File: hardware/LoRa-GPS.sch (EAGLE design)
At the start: 26 parts, among them J2 MF-CON-MICROUSB-RIGHT, U1 MCP1703-3302E/CB, Y1 CRYSTAL.ABS07

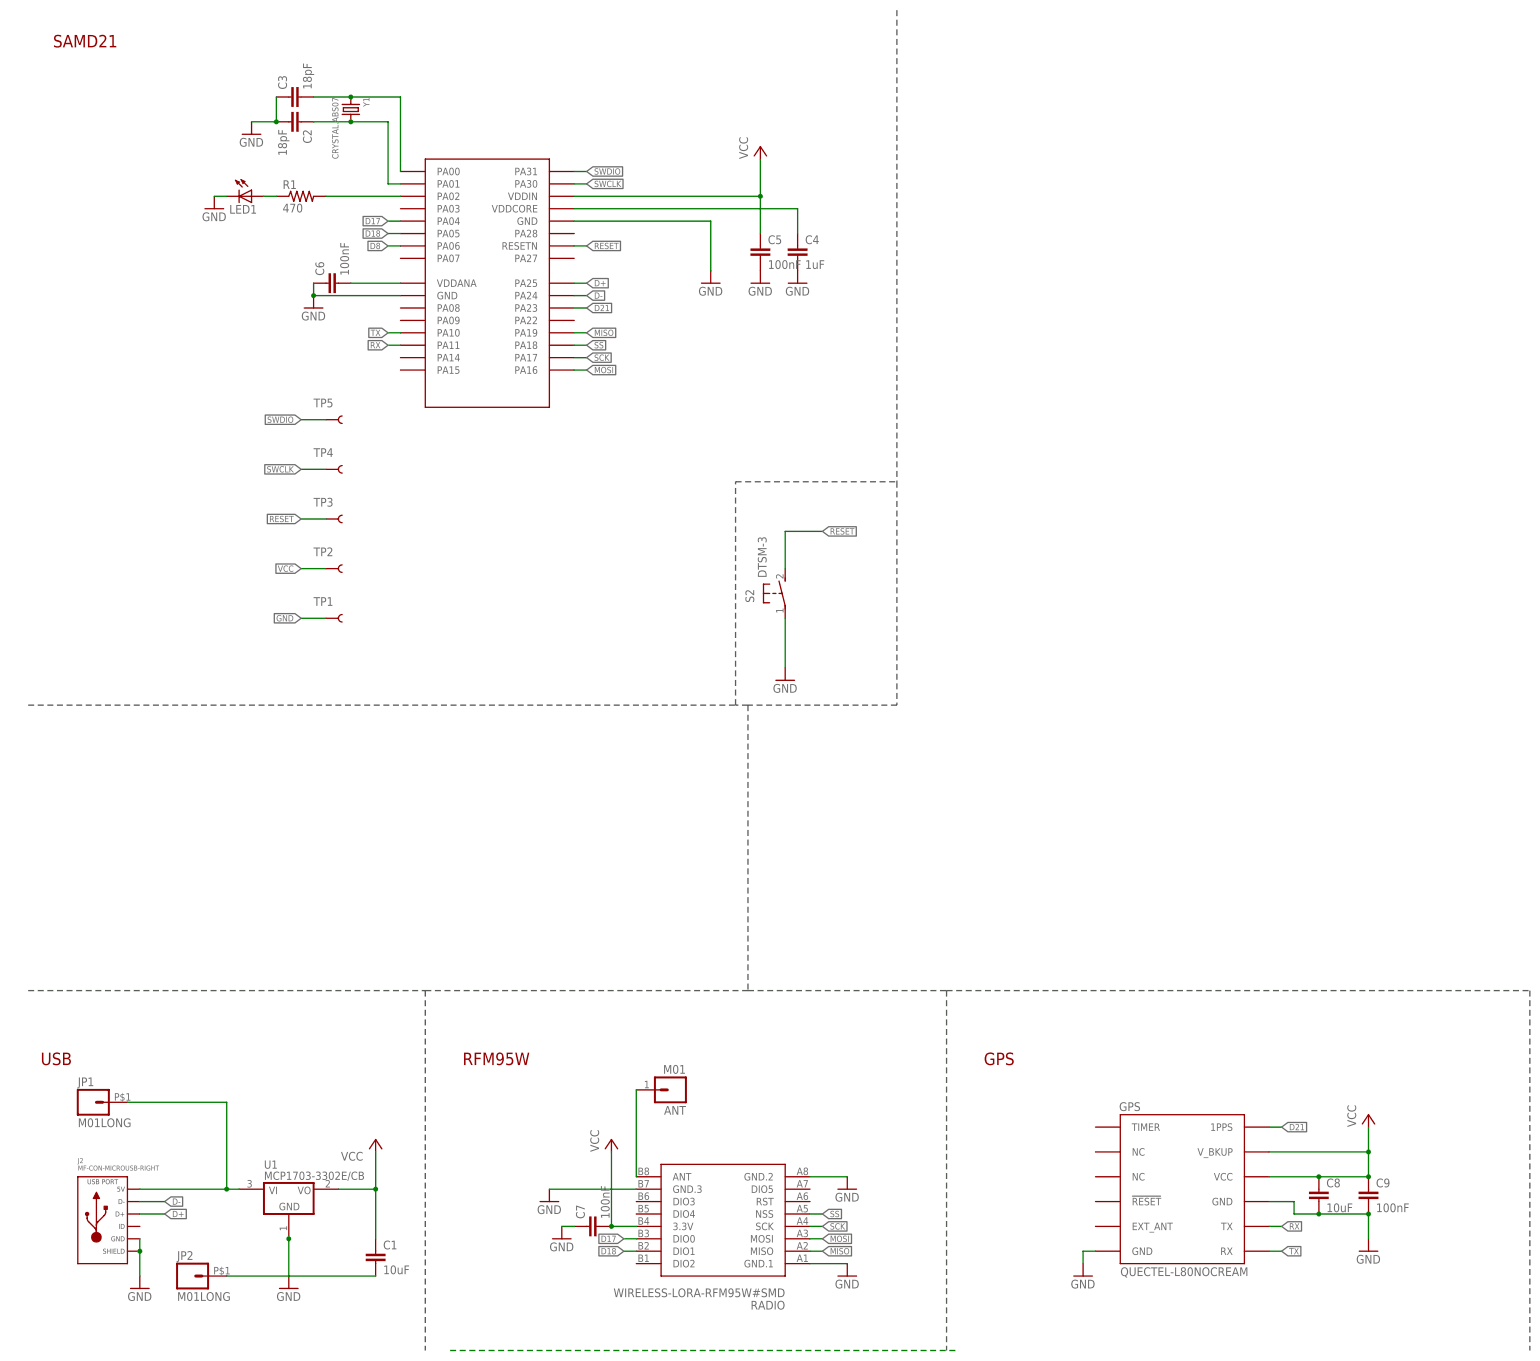
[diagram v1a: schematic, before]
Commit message: add GPS VCC switch - check CPU pin is ok?
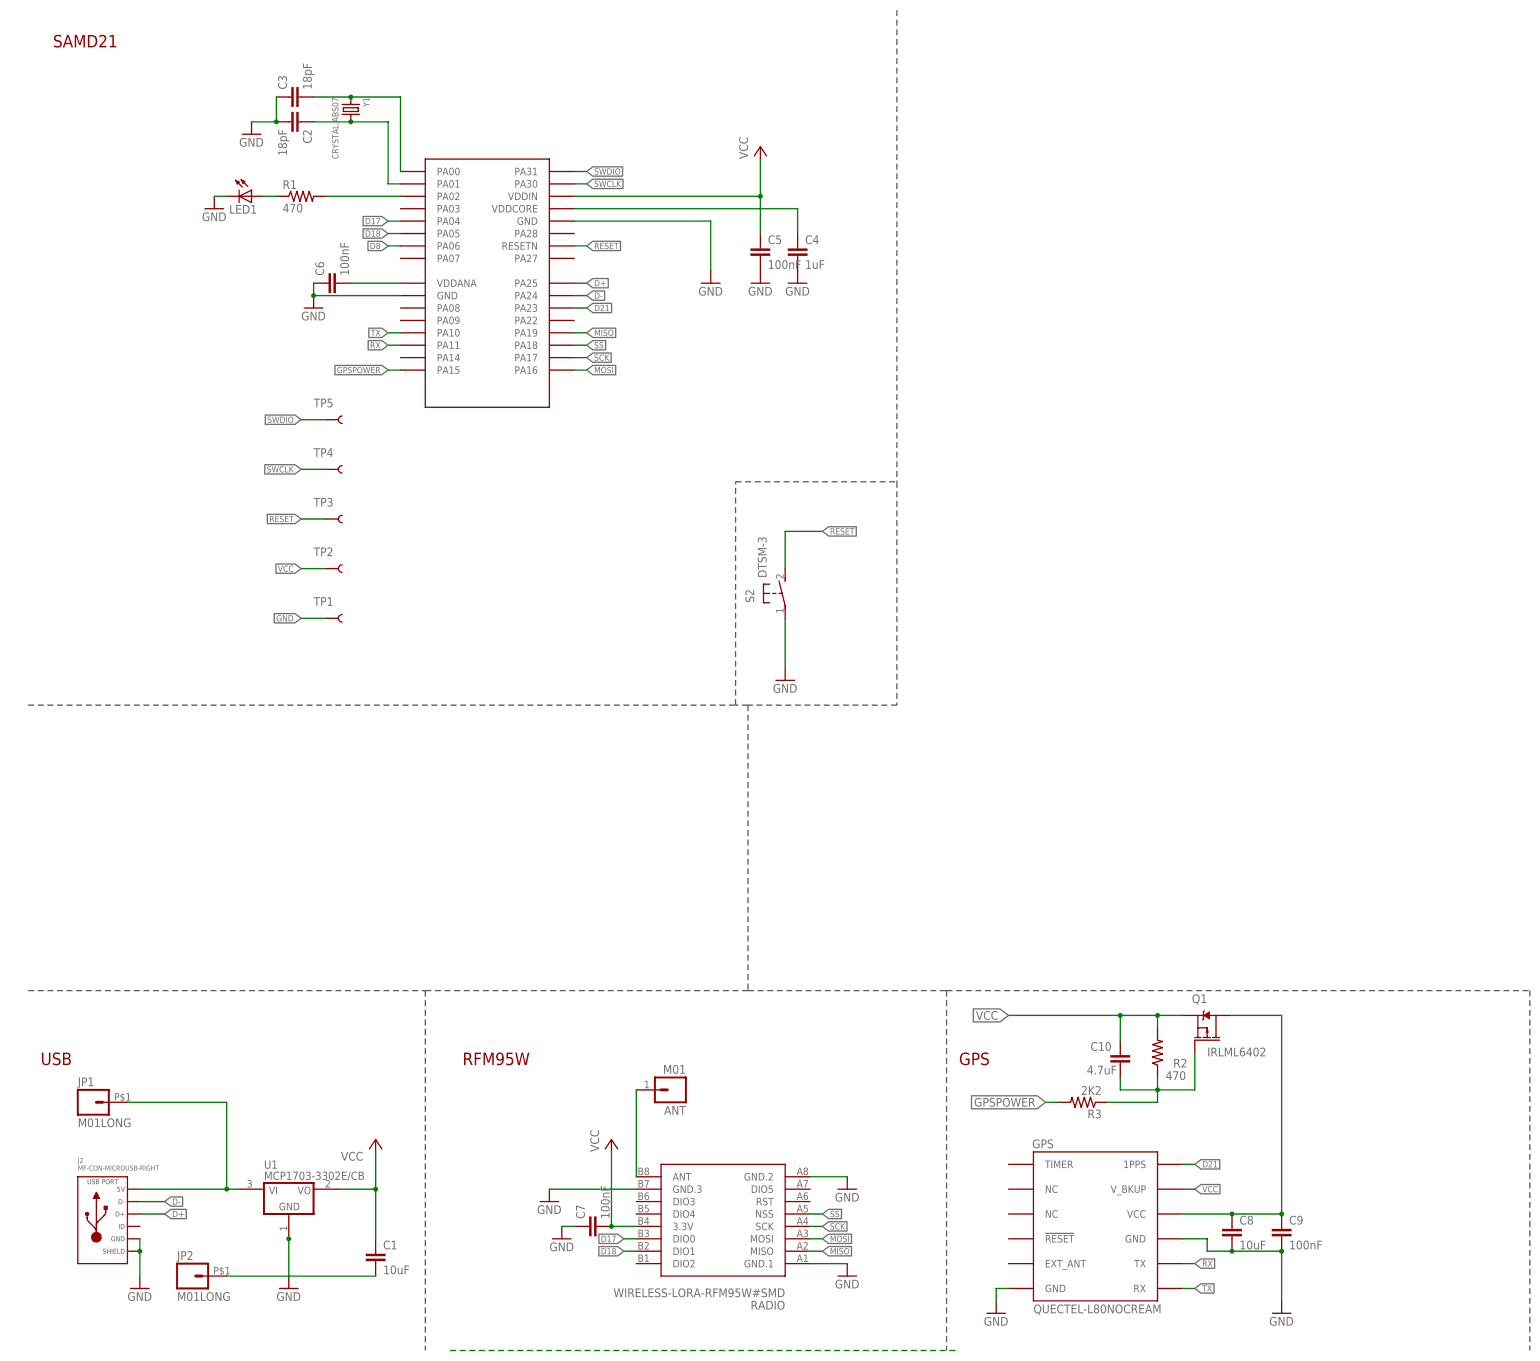
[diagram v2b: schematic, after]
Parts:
- added C10: 4.7uF, nootropicdesign:CAPC0603-THINCREAM
- added Q1: IRLML6402, ianc:MOSFET_PCH-IRLML6402
- added R2: 470, nootropicdesign:R-USR0603-THINCREAM
- added R3: 2K2, nootropicdesign:R-USR0603-THINCREAM
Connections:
- new net GPSPOWER: R3.2, SAMD21.PA15
- new net N$7: C8.1, C9.1, GPS.VCC, Q1.D
- new net N$8: C10.2, Q1.G, R2.1, R3.1
- net VCC: now also C10.1, Q1.S, R2.2; no longer C8.1, C9.1, GPS.VCC
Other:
- moved on the sheet: C8, C9, GPS

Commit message: amph usb conn
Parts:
- removed J2: MF-CON-MICROUSB-RIGHT, nootropicdesign:USB_MICRO_RIGHT
- added J1: 10118193-0001LF, usb:10118193-0001LF
- ANT, C1, C10, C2, C3, C4, C8, GPS, JP1, JP2, LED1, Q1, R1, R2, R3, RADIO, S2, SAMD21, TP1, TP2, TP3, TP4, TP5, U1, Y1: OC_FARNELL (none) -> unknown
- C5, C6, C7, C9: MF (none) -> AVX; MPN (none) -> 02016D104KAT2A; OC_FARNELL (none) -> 1657913
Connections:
- net D+: now also J1.3; no longer J2.D+
- net D-: now also J1.2; no longer J2.D-
- net GND: now also J1.5; no longer J2.GND, J2.SLD
- net VIN: now also J1.1; no longer J2.5V

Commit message: 470 to 47k
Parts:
- R2: value 470 -> 47k
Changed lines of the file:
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@@
 <attribute name="OC_FARNELL" value="unknown"/>
 </part>
-<part name="R2" library="nootropicdesign" deviceset="R-US" device="R0603-THINCREAM" value="470">
+<part name="R2" library="nootropicdesign" deviceset="R-US" device="R0603-THINCREAM" value="47k">
 <attribute name="MF" value=""/>
 <attribute name="MPN" value=""/>

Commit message: sma
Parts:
- removed J1: 10118193-0001LF, usb:10118193-0001LF
- added J2: CON-SMA-EDGE-S, CON-SMA-EDGE-S:CON-SMA-EDGE-S
- added J3: USB3085-XX-X_REVD, USB3085-XX-X_REVD:USB3085-XX-X_REVD
- ANT: value M01 -> (none); device nootropicdesign:M01 -> wirepad:1,6/0,8; OC_FARNELL unknown -> (none)
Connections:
- net ANT: now also ANT.P, J2.1; no longer ANT.1
- net D+: now also J3.D+; no longer J1.3
- net D-: now also J3.D-; no longer J1.2
- net GND: now also J2.2, J3.GND; no longer J1.5
- net VIN: now also J3.VBUS; no longer J1.1
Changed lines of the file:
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@@
 <layer number="2" name="Route2" color="1" fill="3" visible="no" active="no"/>
 <layer number="3" name="Route3" color="4" fill="3" visible="no" active="no"/>
+<layer number="4" name="Route4" color="1" fill="4" visible="no" active="no"/>
+<layer number="5" name="Route5" color="4" fill="4" visible="no" active="no"/>
+<layer number="6" name="Route6" color="1" fill="8" visible="no" active="no"/>
+<layer number="7" name="Route7" color="4" fill="8" visible="no" active="no"/>
+<layer number="8" name="Route8" color="1" fill="2" visible="no" active="no"/>
+<layer number="9" name="Route9" color="4" fill="2" visible="no" active="no"/>
+<layer number="10" name="Route10" color="1" fill="7" visible="no" active="no"/>
+<layer number="11" name="Route11" color="4" fill="7" visible="no" active="no"/>
+<layer number="12" name="Route12" color="1" fill="5" visible="no" active="no"/>
+<layer number="13" name="Route13" color="4" fill="5" visible="no" active="no"/>
 <layer number="14" name="Route14" color="1" fill="6" visible="no" active="no"/>
 <layer number="15" name="Route15" color="4" fill="6" visible="no" active="no"/>
@@
 </part>
 <part name="GND16" library="supply1" deviceset="GND" device=""/>
-<part name="ANT" library="nootropicdesign" deviceset="M01" device="">
-<attribute name="MF" value=""/>
-<attribute name="MPN" value=""/>
-<attribute name="OC_FARNELL" value="unknown"/>
-</part>
 <part name="TP5" library="SparkFun-Passives" deviceset="TEST-POINT" device="3X5" value="">
 <attribute name="MF" value=""/>
@@
 <attribute name="OC_FARNELL" value="unknown"/>
 </part>
-<part name="J1" library="usb" deviceset="10118193-0001LF" device=""/>
+<part name="J2" library="CON-SMA-EDGE-S" deviceset="CON-SMA-EDGE-S" device=""/>
+<part name="GND6" library="supply1" deviceset="GND" device=""/>
+<part name="ANT" library="wirepad" library_urn="urn:adsk.eagle:library:412" deviceset="1,6/0,8" device="" package3d_urn="urn:adsk.eagle:package:30830/1"/>
+<part name="J3" library="USB3085-XX-X_REVD" deviceset="USB3085-XX-X_REVD" device=""/>
 </parts>
 <sheets>
@@
 <attribute name="VALUE" x="-22.86" y="-144.78" size="1.778" layer="96"/>
 </instance>
-<instance part="ANT" gate="G$1" x="-144.78" y="-96.52" smashed="yes" rot="R180">
-<attribute name="VALUE" x="-142.24" y="-91.44" size="1.778" layer="96" rot="R180"/>
-<attribute name="NAME" x="-142.24" y="-99.822" size="1.778" layer="95" rot="R180"/>
-<attribute name="OC_FARNELL" x="-144.78" y="-96.52" size="1.778" layer="96" display="off"/>
-<attribute name="MF" x="-144.78" y="-96.52" size="1.778" layer="96" display="off"/>
-<attribute name="MPN" x="-144.78" y="-96.52" size="1.778" layer="96" display="off"/>
-</instance>
 <instance part="TP5" gate="G$1" x="-215.9" y="40.64" smashed="yes">
 <attribute name="NAME" x="-218.44" y="43.18" size="1.778" layer="95"/>
@@
 <attribute name="MPN" x="-60.96" y="-99.06" size="1.778" layer="96" display="off"/>
 </instance>
-<instance part="J1" gate="A" x="-259.08" y="-116.84" smashed="yes" rot="MR0">
-<attribute name="NAME" x="-263.2456" y="-111.5314" size="2.0828" layer="95" ratio="6" rot="SMR0"/>
+<instance part="J2" gate="G$1" x="-165.1" y="-93.98" smashed="yes">
+<attribute name="NAME" x="-168.91" y="-89.916" size="1.778" layer="95"/>
+<attribute name="VALUE" x="-164.084" y="-88.138" size="1.778" layer="96"/>
+</instance>
+<instance part="GND6" gate="1" x="-157.48" y="-101.6" smashed="yes">
+<attribute name="VALUE" x="-160.02" y="-104.14" size="1.778" layer="96"/>
+</instance>
+<instance part="ANT" gate="P" x="-142.24" y="-91.44" smashed="yes" rot="R180">
+<attribute name="NAME" x="-141.097" y="-93.2942" size="1.778" layer="95" rot="R180"/>
+<attribute name="VALUE" x="-141.097" y="-88.138" size="1.778" layer="96" rot="R180"/>
+</instance>
+<instance part="J3" gate="G$1" x="-271.78" y="-124.46" smashed="yes" rot="MR0">
+<attribute name="NAME" x="-266.696890625" y="-113.7855" size="1.779090625" layer="95" rot="MR0"/>
+<attribute name="VALUE" x="-251.452190625" y="-147.3395" size="1.78073125" layer="96" rot="MR0"/>
 </instance>
 </instances>
@@
 <wire x1="-254" y1="-127" x2="-254" y2="-134.62" width="0.1524" layer="91"/>
 <pinref part="GND9" gate="1" pin="GND"/>
-<pinref part="J1" gate="A" pin="5"/>
-<wire x1="-259.08" y1="-127" x2="-254" y2="-127" width="0.1524" layer="91"/>
+<wire x1="-261.62" y1="-127" x2="-254" y2="-127" width="0.1524" layer="91"/>
+<pinref part="J3" gate="G$1" pin="GND"/>
 </segment>
 <segment>
@@
 <label x="-220.98" y="0" size="1.27" layer="95" rot="R180" xref="yes"/>
 </segment>
+<segment>
+<pinref part="GND6" gate="1" pin="GND"/>
+<pinref part="J2" gate="G$1" pin="2"/>
+<wire x1="-157.48" y1="-99.06" x2="-157.48" y2="-93.98" width="0.1524" layer="91"/>
+<wire x1="-157.48" y1="-93.98" x2="-162.56" y2="-93.98" width="0.1524" layer="91"/>
+</segment>
 </net>
 <net name="VCC" class="0">
@@
 <segment>
 <pinref part="U1" gate="G$1" pin="VI"/>
-<wire x1="-259.08" y1="-116.84" x2="-236.22" y2="-116.84" width="0.1524" layer="91"/>
+<wire x1="-261.62" y1="-116.84" x2="-236.22" y2="-116.84" width="0.1524" layer="91"/>
 <wire x1="-236.22" y1="-116.84" x2="-233.68" y2="-116.84" width="0.1524" layer="91"/>
 <pinref part="JP1" gate="G$1" pin="1"/>
@@
 <wire x1="-236.22" y1="-99.06" x2="-236.22" y2="-116.84" width="0.1524" layer="91"/>
 <junction x="-236.22" y="-116.84"/>
-<pinref part="J1" gate="A" pin="1"/>
+<pinref part="J3" gate="G$1" pin="VBUS"/>
 </segment>
 </net>
@@
 <segment>
 <label x="-248.92" y="-119.38" size="1.27" layer="95" xref="yes"/>
-<pinref part="J1" gate="A" pin="2"/>
-<wire x1="-259.08" y1="-119.38" x2="-248.92" y2="-119.38" width="0.1524" layer="91"/>
+<wire x1="-261.62" y1="-119.38" x2="-248.92" y2="-119.38" width="0.1524" layer="91"/>
+<pinref part="J3" gate="G$1" pin="D-"/>
 </segment>
 <segment>
@@
 <segment>
 <label x="-248.92" y="-121.92" size="1.27" layer="95" xref="yes"/>
-<pinref part="J1" gate="A" pin="3"/>
-<wire x1="-259.08" y1="-121.92" x2="-248.92" y2="-121.92" width="0.1524" layer="91"/>
+<wire x1="-261.62" y1="-121.92" x2="-248.92" y2="-121.92" width="0.1524" layer="91"/>
+<pinref part="J3" gate="G$1" pin="D+"/>
 </segment>
 <segment>
@@
 <segment>
 <pinref part="RADIO" gate="G$1" pin="ANT"/>
-<pinref part="ANT" gate="G$1" pin="1"/>
-<wire x1="-152.4" y1="-114.3" x2="-152.4" y2="-96.52" width="0.1524" layer="91"/>
-</segment>
-</net>
+<wire x1="-152.4" y1="-114.3" x2="-152.4" y2="-91.44" width="0.1524" layer="91"/>
+<pinref part="J2" gate="G$1" pin="1"/>
+<wire x1="-152.4" y1="-91.44" x2="-162.56" y2="-91.44" width="0.1524" layer="91"/>
+<pinref part="ANT" gate="P" pin="P"/>
+<wire x1="-152.4" y1="-91.44" x2="-144.78" y2="-91.44" width="0.1524" layer="91"/>
+<junction x="-152.4" y="-91.44"/>
+</segment>
+</net>

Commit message: DRC pass
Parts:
- removed S2: DTSM-3, switch-tact:DTSM-3
- added S1: SKTHACE010, SamacSys_Parts:SKTHACE010
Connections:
- net GND: now also S1.2, S1.4; no longer S2.1
- net RESET: now also S1.1, S1.3; no longer S2.2
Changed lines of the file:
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@@
-<attribute name="OC_FARNELL" value="unknown"/>
-</part>
-<part name="S2" library="switch-tact" deviceset="DTSM-3" device="">
-<attribute name="MF" value=""/>
-<attribute name="MPN" value=""/>
 <attribute name="OC_FARNELL" value="unknown"/>
 </part>
@@
 <part name="ANT" library="wirepad" library_urn="urn:adsk.eagle:library:412" deviceset="1,6/0,8" device="" package3d_urn="urn:adsk.eagle:package:30830/1"/>
 <part name="J3" library="USB3085-XX-X_REVD" deviceset="USB3085-XX-X_REVD" device=""/>
+<part name="S1" library="SamacSys_Parts" deviceset="SKTHACE010" device=""/>
 </parts>
 <sheets>
@@
 <attribute name="MPN" x="-243.84" y="-134.62" size="1.778" layer="96" display="off"/>
 </instance>
-<instance part="S2" gate="G$1" x="-121.92" y="5.08" smashed="yes">
-<attribute name="NAME" x="-128.27" y="3.175" size="1.778" layer="95" rot="R90"/>
-<attribute name="VALUE" x="-125.73" y="8.255" size="1.778" layer="96" rot="R90"/>
-<attribute name="OC_FARNELL" x="-121.92" y="5.08" size="1.778" layer="96" display="off"/>
-<attribute name="MF" x="-121.92" y="5.08" size="1.778" layer="96" display="off"/>
-<attribute name="MPN" x="-121.92" y="5.08" size="1.778" layer="96" display="off"/>
-</instance>
 <instance part="GND15" gate="1" x="-121.92" y="-12.7" smashed="yes">
 <attribute name="VALUE" x="-124.46" y="-15.24" size="1.778" layer="96"/>
@@
 <attribute name="NAME" x="-266.696890625" y="-113.7855" size="1.779090625" layer="95" rot="MR0"/>
 <attribute name="VALUE" x="-251.452190625" y="-147.3395" size="1.78073125" layer="96" rot="MR0"/>
+</instance>
+<instance part="S1" gate="G$1" x="-127" y="0" smashed="yes">
+<attribute name="NAME" x="-110.49" y="7.62" size="1.778" layer="95" align="center-left"/>
+<attribute name="VALUE" x="-110.49" y="5.08" size="1.778" layer="96" align="center-left"/>
 </instance>
 </instances>
@@
 </segment>
 <segment>
-<pinref part="GND15" gate="1" pin="GND"/>
-<pinref part="S2" gate="G$1" pin="1"/>
-<wire x1="-121.92" y1="-10.16" x2="-121.92" y2="0" width="0.1524" layer="91"/>
-</segment>
-<segment>
 <pinref part="SAMD21" gate="G$1" pin="GND@2"/>
 <wire x1="-165.1" y1="81.28" x2="-137.16" y2="81.28" width="0.1524" layer="91"/>
@@
 <wire x1="-157.48" y1="-99.06" x2="-157.48" y2="-93.98" width="0.1524" layer="91"/>
 <wire x1="-157.48" y1="-93.98" x2="-162.56" y2="-93.98" width="0.1524" layer="91"/>
+</segment>
+<segment>
+<pinref part="GND15" gate="1" pin="GND"/>
+<pinref part="S1" gate="G$1" pin="2"/>
+<wire x1="-121.92" y1="-10.16" x2="-106.68" y2="-10.16" width="0.1524" layer="91"/>
+<wire x1="-106.68" y1="-10.16" x2="-106.68" y2="-2.54" width="0.1524" layer="91"/>
+<pinref part="S1" gate="G$1" pin="4"/>
+<wire x1="-106.68" y1="-2.54" x2="-106.68" y2="0" width="0.1524" layer="91"/>
+<junction x="-106.68" y="-2.54"/>
 </segment>
 </net>
@@
 </segment>
 <segment>
-<pinref part="S2" gate="G$1" pin="2"/>
 <wire x1="-121.92" y1="10.16" x2="-121.92" y2="17.78" width="0.1524" layer="91"/>
 <wire x1="-121.92" y1="17.78" x2="-114.3" y2="17.78" width="0.1524" layer="91"/>
 <label x="-114.3" y="17.78" size="1.27" layer="95" xref="yes"/>
-</segment>
-</net>
+<pinref part="S1" gate="G$1" pin="3"/>
+<wire x1="-121.92" y1="10.16" x2="-127" y2="10.16" width="0.1524" layer="91"/>
+<wire x1="-127" y1="10.16" x2="-127" y2="0" width="0.1524" layer="91"/>
+<pinref part="S1" gate="G$1" pin="1"/>
+<wire x1="-127" y1="-2.54" x2="-127" y2="0" width="0.1524" layer="91"/>
+<junction x="-127" y="0"/>
+</segment>
+</net>
